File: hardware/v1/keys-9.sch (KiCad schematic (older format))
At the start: 11 parts, among them P1 CONN_01X04, SW1_READ1 SWITCH_INV, SW2_SINGLE_READ1 SWITCH_INV, SW3_PUNCH1 SWITCH_INV, SW4_PROGDISP1 SWITCH_INV, SW5_TIL1 SWITCH_INV, SW6_INIT1 SWITCH_INV, SW7_CLEAR1 SWITCH_INV, SW8_EXTTREE1 SWITCH_INV, SW9_SINGLESHOT1 SWITCH_INV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

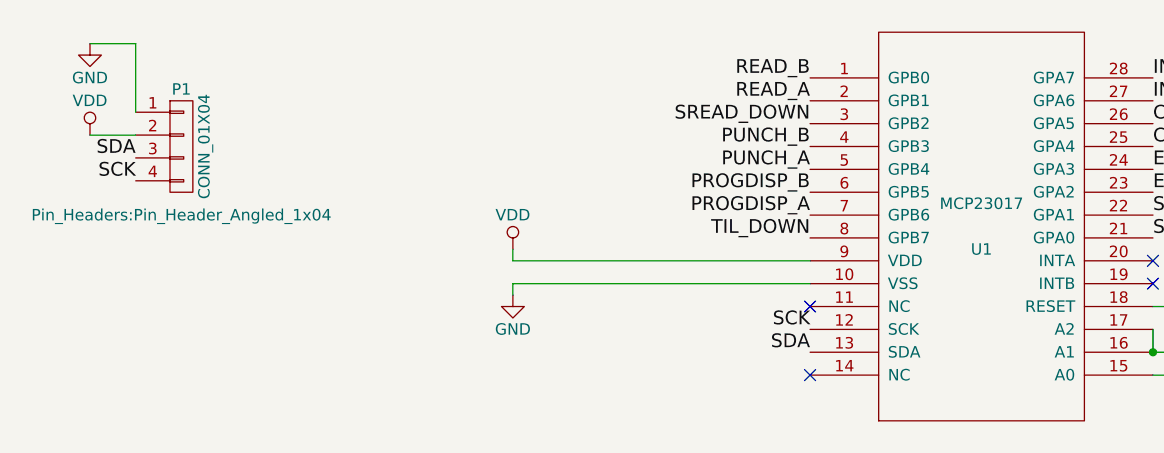
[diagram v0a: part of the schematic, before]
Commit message: Add pcbs and cutouts for magnetic drum store status lamps (not labelled).
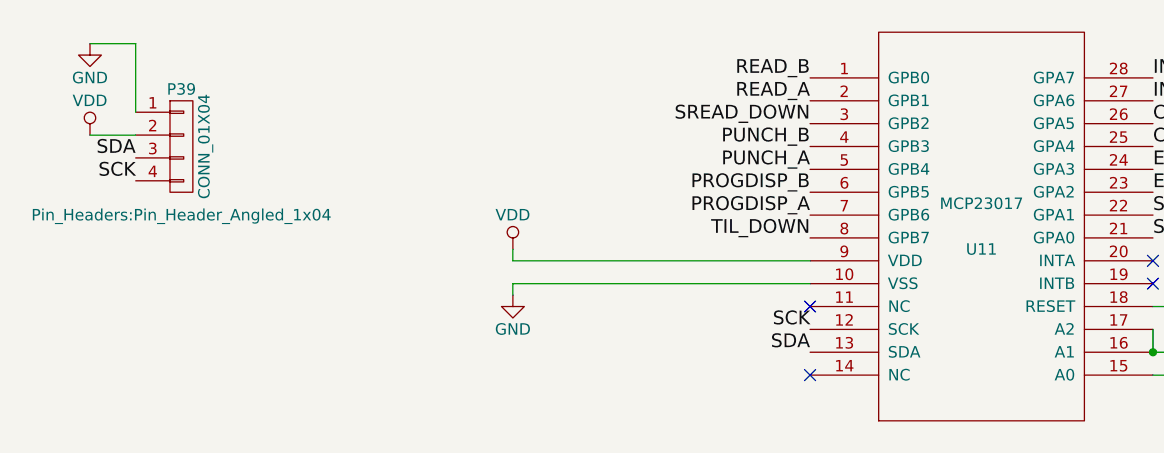
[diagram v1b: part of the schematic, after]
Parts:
- renumbered P1 to P39, U1 to U11
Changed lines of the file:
@@
 $Descr A4 11693 8268
 encoding utf-8
-Sheet 1 31
+Sheet 1 36
 Title ""
 Date ""
@@
 Connection ~ 9450 3400
 $Comp
-L GND #PWR01
+L GND #PWR61
 U 1 1 57ABB26D
 P 3100 2850
-F 0 "#PWR01" H 3100 2600 50  0001 C CNN
+F 0 "#PWR61" H 3100 2600 50  0001 C CNN
 F 1 "GND" H 3100 2700 50  0000 C CNN
 F 2 "" H 3100 2850 50  0000 C CNN
@@
 NoConn ~ 4400 3200
 $Comp
-L VDD #PWR02
+L VDD #PWR60
 U 1 1 57ABB279
 P 3100 2650
-F 0 "#PWR02" H 3100 2500 50  0001 C CNN
+F 0 "#PWR60" H 3100 2500 50  0001 C CNN
 F 1 "VDD" H 3100 2800 50  0000 C CNN
 F 2 "" H 3100 2650 50  0000 C CNN
@@
 	3100 2700 3100 2650
 $Comp
-L VDD #PWR03
+L VDD #PWR59
 U 1 1 57ABB283
 P 1250 2150
-F 0 "#PWR03" H 1250 2000 50  0001 C CNN
+F 0 "#PWR59" H 1250 2000 50  0001 C CNN
 F 1 "VDD" H 1250 2300 50  0000 C CNN
 F 2 "" H 1250 2150 50  0000 C CNN
@@
 $EndComp
 $Comp
-L GND #PWR04
+L GND #PWR58
 U 1 1 57ABB289
 P 1250 1750
-F 0 "#PWR04" H 1250 1500 50  0001 C CNN
+F 0 "#PWR58" H 1250 1500 50  0001 C CNN
 F 1 "GND" H 1250 1600 50  0000 C CNN
 F 2 "" H 1250 1750 50  0000 C CNN
@@
 SCK
 $Comp
-L CONN_01X04 P1
+L CONN_01X04 P39
 U 1 1 57ABB291
 P 1650 2200
-F 0 "P1" H 1650 2450 50  0000 C CNN
+F 0 "P39" H 1650 2450 50  0000 C CNN
 F 1 "CONN_01X04" V 1750 2200 50  0000 C CNN
 F 2 "Pin_Headers:Pin_Header_Angled_1x04" H 1650 1900 50  0000 C CNN
@@
 SCK
 $Comp
-L VDD #PWR05
+L VDD #PWR63
 U 1 1 57ABB29D
 P 6300 2850
-F 0 "#PWR05" H 6300 2700 50  0001 C CNN
+F 0 "#PWR63" H 6300 2700 50  0001 C CNN
 F 1 "VDD" H 6300 3000 50  0000 C CNN
 F 2 "" H 6300 2850 50  0000 C CNN
@@
 	6300 2900 5900 2900
 $Comp
-L GND #PWR06
+L GND #PWR62
 U 1 1 57ABB2A5
 P 6100 3350
-F 0 "#PWR06" H 6100 3100 50  0001 C CNN
+F 0 "#PWR62" H 6100 3100 50  0001 C CNN
 F 1 "GND" H 6100 3200 50  0000 C CNN
 F 2 "" H 6100 3350 50  0000 C CNN
@@
 Connection ~ 9450 5300
 $Comp
-L GND #PWR07
+L GND #PWR64
 U 1 1 57ABB3DD
 P 9450 6100
-F 0 "#PWR07" H 9450 5850 50  0001 C CNN
+F 0 "#PWR64" H 9450 5850 50  0001 C CNN
 F 1 "GND" H 9450 5950 50  0000 C CNN
 F 2 "" H 9450 6100 50  0000 C CNN
@@
 SINGLE_B
 $Comp
-L MCP23017 U1
+L MCP23017 U11
 U 1 1 57ABB2CD
 P 5150 2550
-F 0 "U1" H 5150 2450 50  0000 C CNN
+F 0 "U11" H 5150 2450 50  0000 C CNN
 F 1 "MCP23017" H 5150 2650 50  0000 C CNN
 F 2 "DIL28:DIL28" H 5150 2550 50  0001 C CNN
